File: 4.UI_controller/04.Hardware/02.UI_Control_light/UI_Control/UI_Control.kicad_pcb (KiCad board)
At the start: 2 copper layers, 63 x 32 mm, 28 parts, among them J2 USB_B_Mini, J3 LCD, J4 Conn_01x03_Male, J5 SWD, Q2 DMN6140L, U1 STM32L412K8Tx, U3 MCP1812BT_033TT, U4 MCP4725A, U5 TCA9534, U6 OPA2990

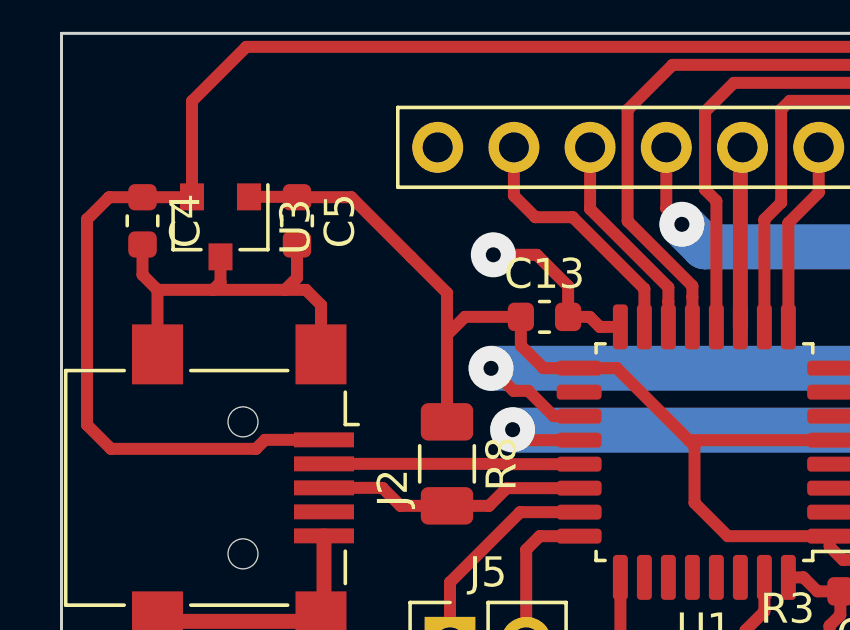
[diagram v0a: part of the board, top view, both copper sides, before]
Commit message: add graphic function
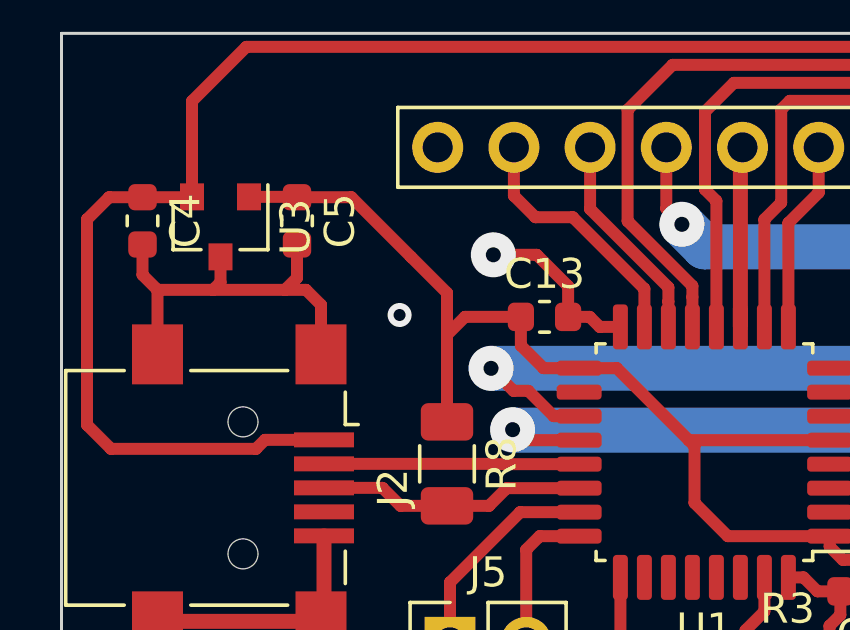
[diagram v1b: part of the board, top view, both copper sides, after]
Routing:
- net GND: vias 8 -> 9
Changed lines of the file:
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@@
     (thickness 1.6)
     (drawings 6)
-    (tracks 331)
+    (tracks 332)
     (zones 0)
     (modules 28)
@@
   )
   (setup
-    (last_trace_width 1)
+    (last_trace_width 0.25)
     (user_trace_width 0.4)
     (user_trace_width 0.5)
@@
     (pad_to_mask_clearance 0)
     (aux_axis_origin 0 0)
-    (visible_elements FFFFFF7F)
+    (visible_elements 7FFFFFFF)
     (pcbplotparams
       (layerselection 0x010fc_ffffffff)
@@
   (via (at 159.5882 65.405) (size 1.5) (drill 0.5) (layers F.Cu B.Cu) (net 1))
   (via (at 155.0416 71.8058) (size 1.5) (drill 0.5) (layers F.Cu B.Cu) (net 1))
+  (via (at 128.27 56.388) (size 0.8) (drill 0.4) (layers F.Cu B.Cu) (net 1))
   (segment (start 144.7 62.225) (end 144.7 63.2) (width 0.4) (layer F.Cu) (net 2))
   (segment (start 144.575 62.1) (end 144.7 62.225) (width 0.4) (layer F.Cu) (net 2))
